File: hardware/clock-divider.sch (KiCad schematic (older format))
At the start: 82 parts, among them J1 PWR, J10 Conn_01x02, J11 Conn_01x02, J12 Conn_01x01, J2 Serial debug / programming he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, J3 SPI / ICSP header, J4 Conn_01x02, J5 Conn_01x02, J6 Conn_01x02, J7 Conn_01x02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

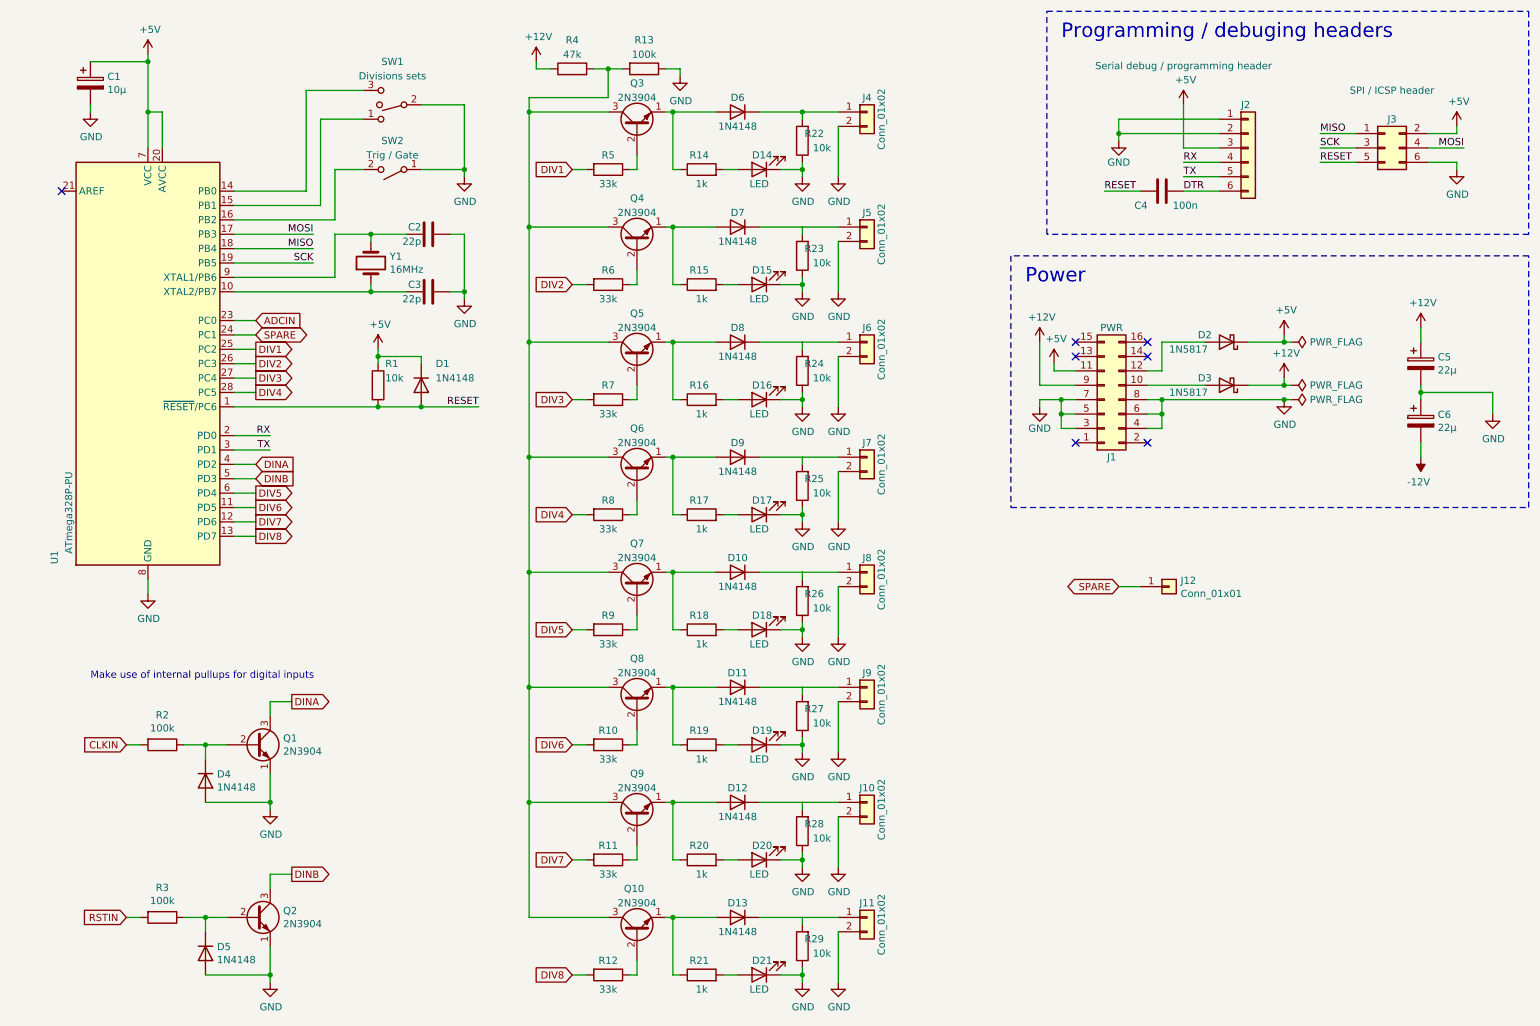
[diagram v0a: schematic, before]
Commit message: Reorganized pins
Reorganized pins on µc and changed µc symbol for a more explicit one
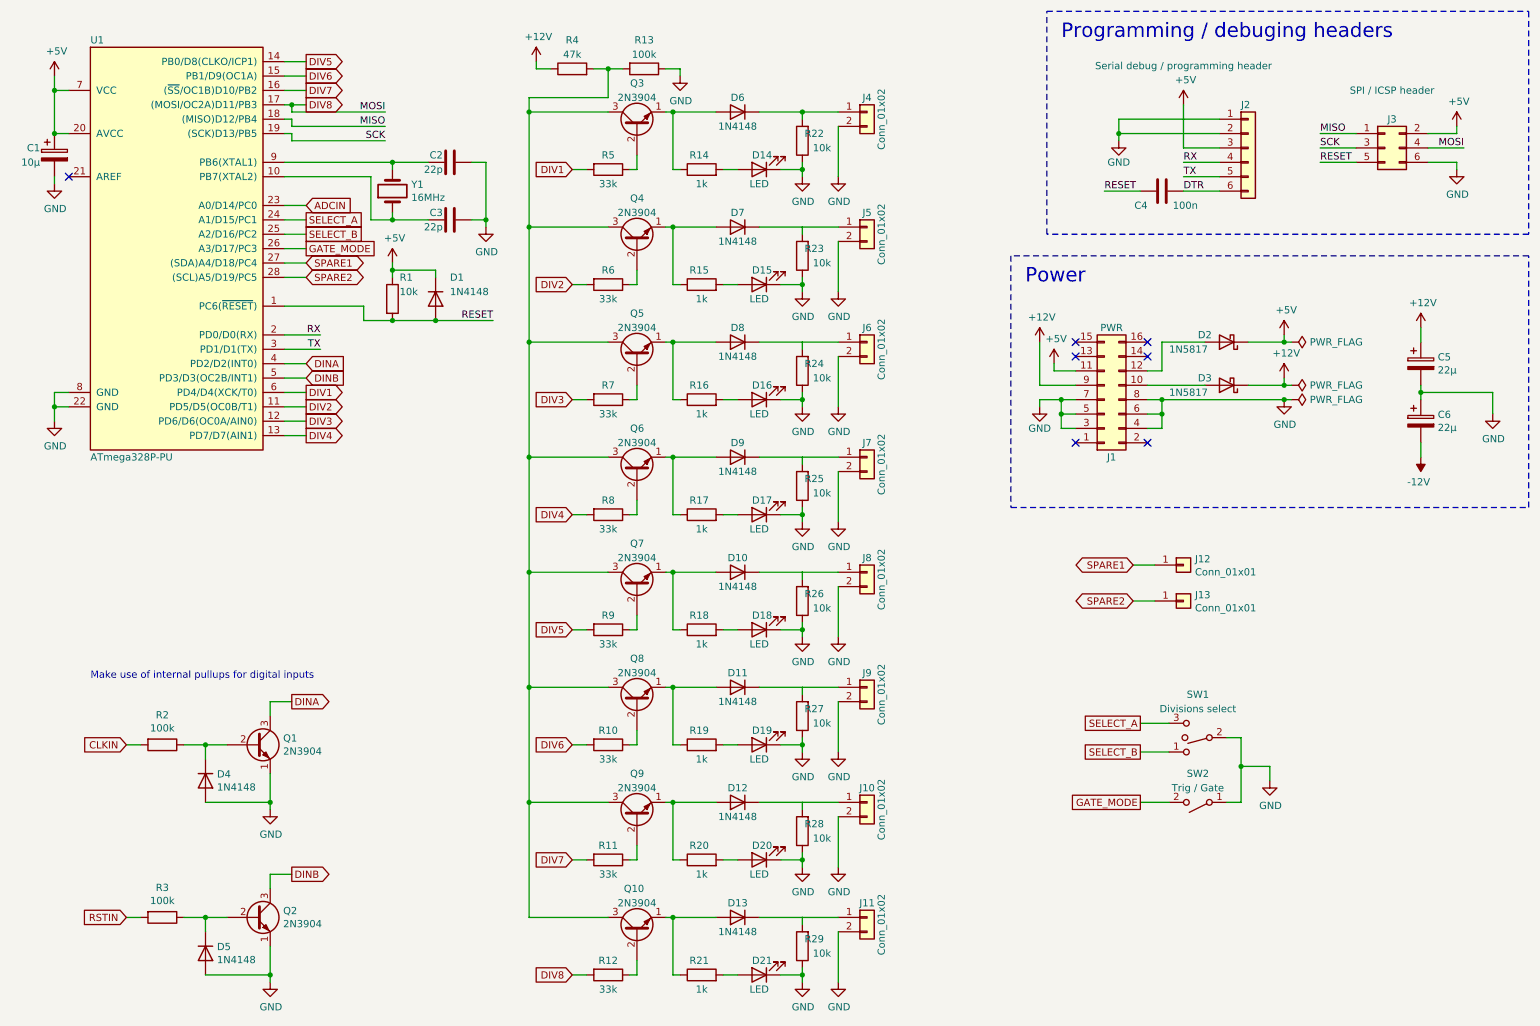
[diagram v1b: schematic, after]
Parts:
- removed U1: ATmega328P-PU, Package_DIP:DIP-28_W7.62mm, symbol MCU_Microchip_ATmega:ATmega328P-PU
- added J13: Conn_01x01, symbol Connector_Generic:Conn_01x01
- added U1: ATmega328P-PU, Housings_DIP:DIP-28_W7.62mm, symbol Custom:AVR_28DIP_Arduino
- SW1: value Divisions sets -> Divisions select
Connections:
- net MOSI is gone; now on net DIV8: J3.4 (Pin_4)
- net +5V: now also U1.20 (AVCC), U1.7 (VCC)
- net ADCIN: now also U1.23 (A0/D14/PC0)
- net DINA: now also U1.4 (PD2/D2(INT0))
- net DINB: now also U1.5 (PD3/D3(OC2B/INT1))
- net DIV1: now also U1.6 (PD4/D4(XCK/T0))
- net DIV2: now also U1.11 (PD5/D5(OC0B/T1))
- net DIV3: now also U1.12 (PD6/D6(OC0A/AIN0))
- net DIV4: now also U1.13 (PD7/D7(AIN1))
- net DIV5: now also U1.14 (PB0/D8(CLKO/ICP1))
- net DIV6: now also U1.15 (PB1/D9(OC1A))
- net DIV7: now also U1.16 ((~SS~/OC1B)D10/PB2)
- net DIV8: now also U1.17 ((MOSI/OC2A)D11/PB3)
- net GND: now also U1.22 (GND), U1.8 (GND)
- net MISO: now also U1.18 ((MISO)D12/PB4)
- net RESET: now also U1.1 (PC6(~RESET~))
- net RX: now also U1.2 (PD0/D0(RX))
- net SCK: now also U1.19 ((SCK)D13/PB5)
- net TX: now also U1.3 (PD1/D1(TX))
- net at C3.2, Y1.1: now also U1.10 (PB7(XTAL2))
- net SELECT_A: now reaches SW1.3
- net SELECT_A: now also U1.24 (A1/D15/PC1)
- net SELECT_B: now reaches SW1.1
- net SELECT_B: now also U1.25 (A2/D16/PC2)
- net GATE_MODE: now reaches SW2.2 (B)
- net GATE_MODE: now also U1.26 (A3/D17/PC3)
- net at C2.2, Y1.2: now also U1.9 (PB6(XTAL1))
- net SPARE renamed SPARE1
- net SPARE1: now also U1.27 ((SDA)A4/D18/PC4)
- new net SPARE2: J13.1 (Pin_1), U1.28 ((SCL)A5/D19/PC5)
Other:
- moved on the sheet: J12

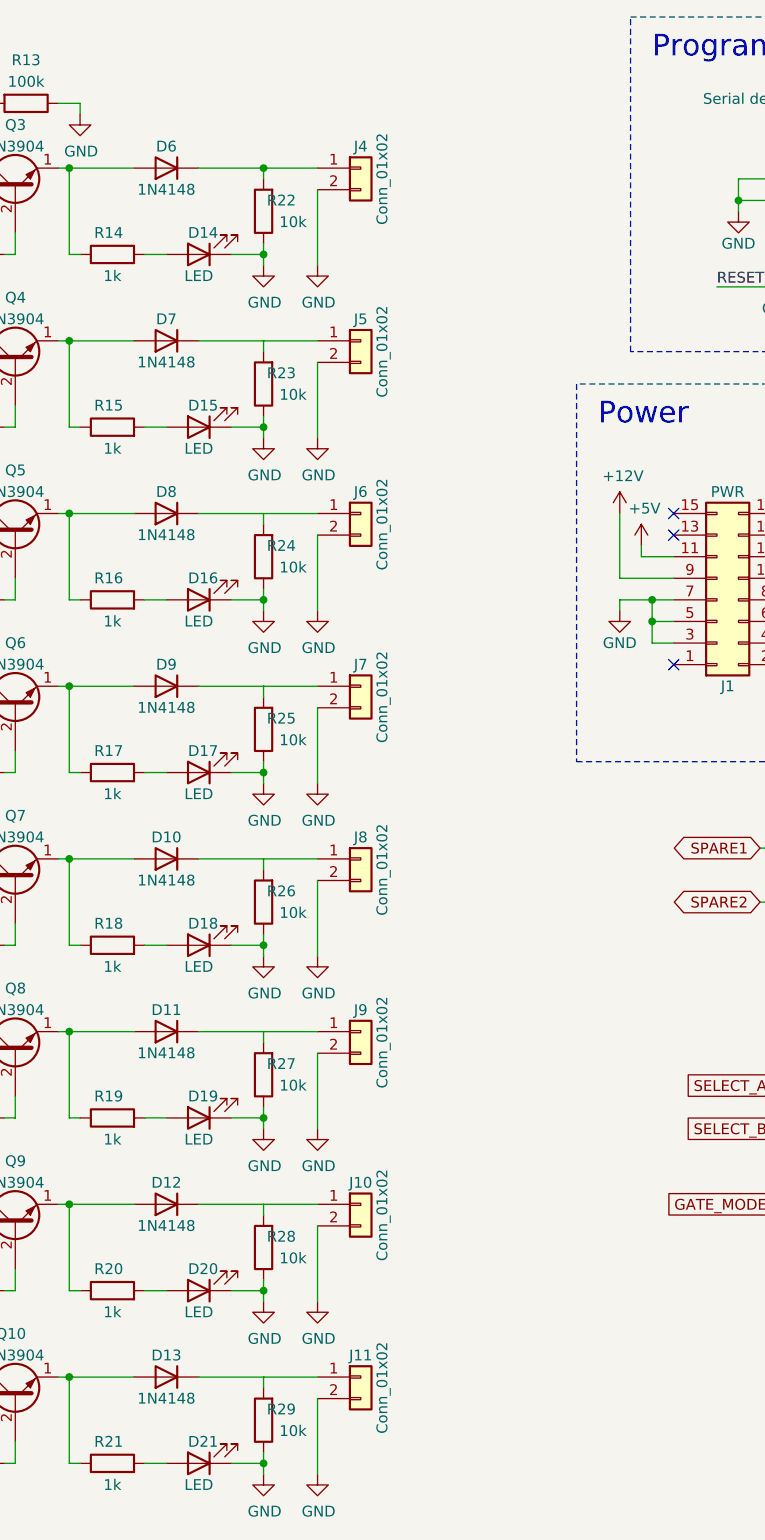
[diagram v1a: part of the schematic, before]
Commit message: Use PJ-302M jack sockets
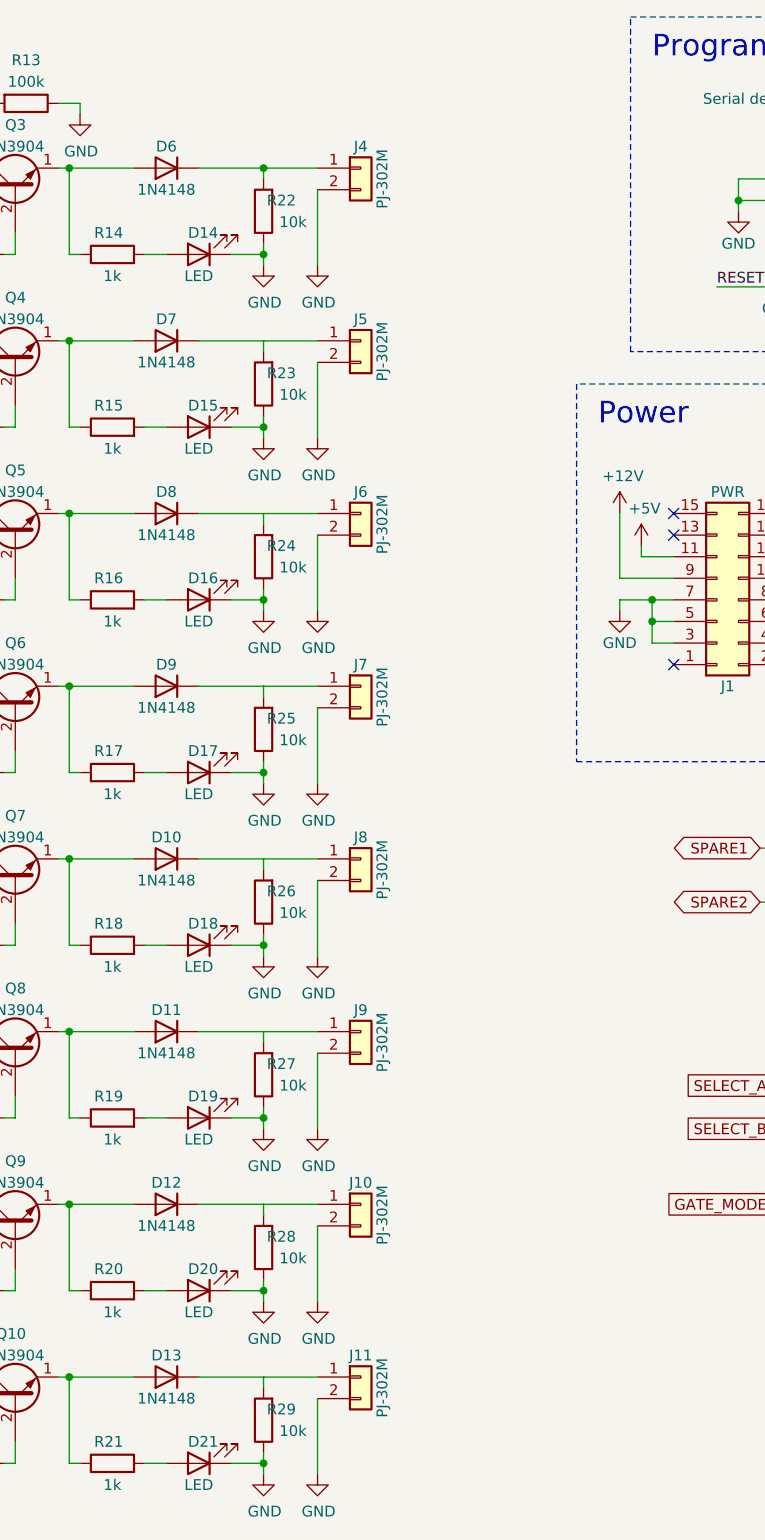
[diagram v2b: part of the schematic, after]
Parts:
- J10, J11, J4, J5, J6, J7, J8, J9: value Conn_01x02 -> PJ-302M
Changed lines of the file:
@@
 P 6450 1300
 F 0 "J4" H 6450 1400 50  0000 C CNN
-F 1 "Conn_01x02" V 6550 1250 50  0000 C CNN
+F 1 "PJ-302M" V 6550 1250 50  0000 C CNN
 F 2 "" H 6450 1300 50  0001 C CNN
 F 3 "~" H 6450 1300 50  0001 C CNN
@@
 P 6450 2100
 F 0 "J5" H 6450 2200 50  0000 C CNN
-F 1 "Conn_01x02" V 6550 2050 50  0000 C CNN
+F 1 "PJ-302M" V 6550 2050 50  0000 C CNN
 F 2 "" H 6450 2100 50  0001 C CNN
 F 3 "~" H 6450 2100 50  0001 C CNN
@@
 P 6450 2900
 F 0 "J6" H 6450 3000 50  0000 C CNN
-F 1 "Conn_01x02" V 6550 2850 50  0000 C CNN
+F 1 "PJ-302M" V 6550 2850 50  0000 C CNN
 F 2 "" H 6450 2900 50  0001 C CNN
 F 3 "~" H 6450 2900 50  0001 C CNN
@@
 P 6450 3700
 F 0 "J7" H 6450 3800 50  0000 C CNN
-F 1 "Conn_01x02" V 6550 3650 50  0000 C CNN
+F 1 "PJ-302M" V 6550 3650 50  0000 C CNN
 F 2 "" H 6450 3700 50  0001 C CNN
 F 3 "~" H 6450 3700 50  0001 C CNN
@@
 P 6450 4500
 F 0 "J8" H 6450 4600 50  0000 C CNN
-F 1 "Conn_01x02" V 6550 4450 50  0000 C CNN
+F 1 "PJ-302M" V 6550 4450 50  0000 C CNN
 F 2 "" H 6450 4500 50  0001 C CNN
 F 3 "~" H 6450 4500 50  0001 C CNN
@@
 P 6450 5300
 F 0 "J9" H 6450 5400 50  0000 C CNN
-F 1 "Conn_01x02" V 6550 5250 50  0000 C CNN
+F 1 "PJ-302M" V 6550 5250 50  0000 C CNN
 F 2 "" H 6450 5300 50  0001 C CNN
 F 3 "~" H 6450 5300 50  0001 C CNN
@@
 P 6450 6100
 F 0 "J10" H 6450 6200 50  0000 C CNN
-F 1 "Conn_01x02" V 6550 6050 50  0000 C CNN
+F 1 "PJ-302M" V 6550 6050 50  0000 C CNN
 F 2 "" H 6450 6100 50  0001 C CNN
 F 3 "~" H 6450 6100 50  0001 C CNN
@@
 P 6450 6900
 F 0 "J11" H 6450 7000 50  0000 C CNN
-F 1 "Conn_01x02" V 6550 6850 50  0000 C CNN
+F 1 "PJ-302M" V 6550 6850 50  0000 C CNN
 F 2 "" H 6450 6900 50  0001 C CNN
 F 3 "~" H 6450 6900 50  0001 C CNN
@@
 $EndComp
 $Comp
-L power:+5V #PWR?
+L power:+5V #PWR06
 U 1 1 6063C1C2
 P 800 1050
-F 0 "#PWR?" H 800 900 50  0001 C CNN
+F 0 "#PWR06" H 800 900 50  0001 C CNN
 F 1 "+5V" H 815 1223 50  0000 C CNN
 F 2 "" H 800 1050 50  0001 C CNN
@@
 $EndComp
 $Comp
-L power:+5V #PWR?
+L power:+5V #PWR030
 U 1 1 6063C1E8
 P 3150 2350
-F 0 "#PWR?" H 3150 2200 50  0001 C CNN
+F 0 "#PWR030" H 3150 2200 50  0001 C CNN
 F 1 "+5V" H 3165 2523 50  0000 C CNN
 F 2 "" H 3150 2350 50  0001 C CNN
@@
 Connection ~ 3150 1650
 $Comp
-L power:GND #PWR?
+L power:GND #PWR031
 U 1 1 6063C21C
 P 3800 2100
-F 0 "#PWR?" H 3800 1850 50  0001 C CNN
+F 0 "#PWR031" H 3800 1850 50  0001 C CNN
 F 1 "GND" H 3805 1927 50  0000 C CNN
 F 2 "" H 3800 2100 50  0001 C CNN
@@
 $EndComp
 $Comp
-L power:GND #PWR?
+L power:GND #PWR028
 U 1 1 6063C222
 P 800 1800
-F 0 "#PWR?" H 800 1550 50  0001 C CNN
+F 0 "#PWR028" H 800 1550 50  0001 C CNN
 F 1 "GND" H 805 1627 50  0000 C CNN
 F 2 "" H 800 1800 50  0001 C CNN
@@
 $EndComp
 $Comp
-L power:GND #PWR?
+L power:GND #PWR029
 U 1 1 6063C228
 P 800 3450
-F 0 "#PWR?" H 800 3200 50  0001 C CNN
+F 0 "#PWR029" H 800 3200 50  0001 C CNN
 F 1 "GND" H 805 3277 50  0000 C CNN
 F 2 "" H 800 3450 50  0001 C CNN
@@
 $EndComp
 $Comp
-L power:GND #PWR?
+L power:GND #PWR032
 U 1 1 6063C245
 P 9250 5950
-F 0 "#PWR?" H 9250 5700 50  0001 C CNN
+F 0 "#PWR032" H 9250 5700 50  0001 C CNN
 F 1 "GND" H 9255 5777 50  0000 C CNN
 F 2 "" H 9250 5950 50  0001 C CNN
